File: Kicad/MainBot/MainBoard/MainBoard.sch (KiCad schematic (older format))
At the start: 35 parts, among them J1 Conn_01x02, J10 Conn_01x24, J11 01x24, J12 Conn_01x05, J13 Conn_01x03, J14 Conn_01x03, J15 Conn_01x03, J16 Conn_01x04, J17 Conn_01x04, J18 Conn_01x04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

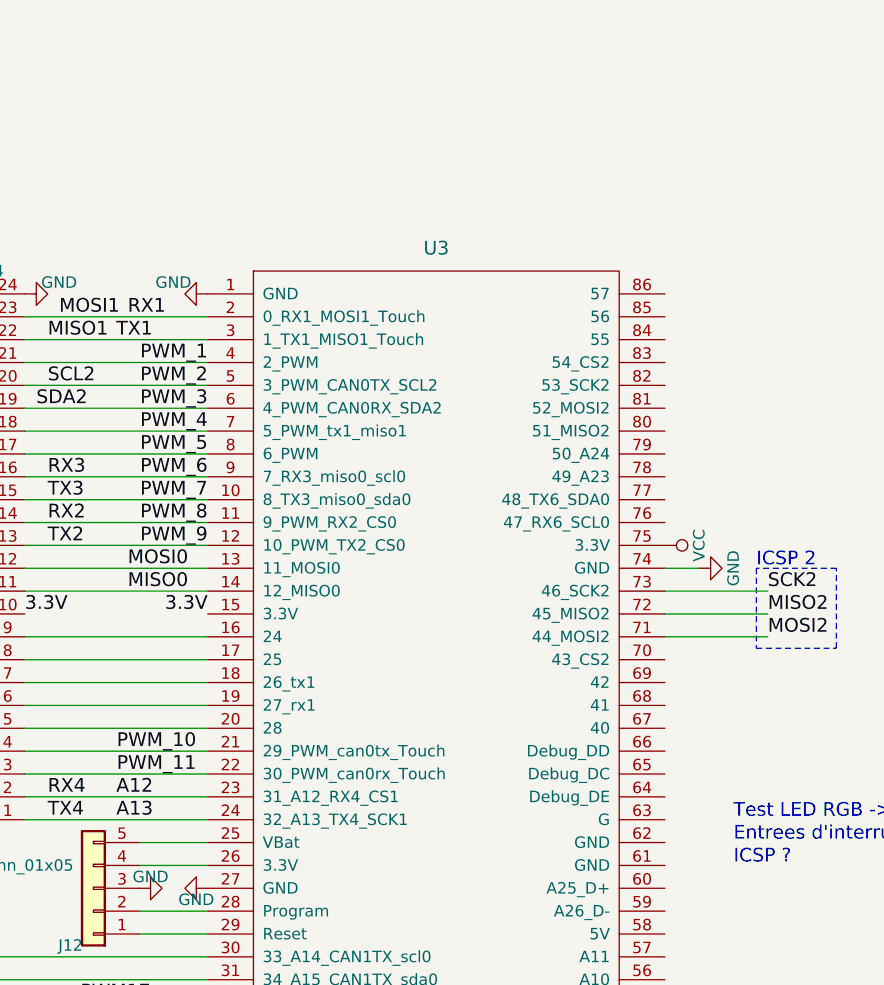
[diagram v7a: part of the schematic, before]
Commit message: Added SPI1 and SPI2 channels
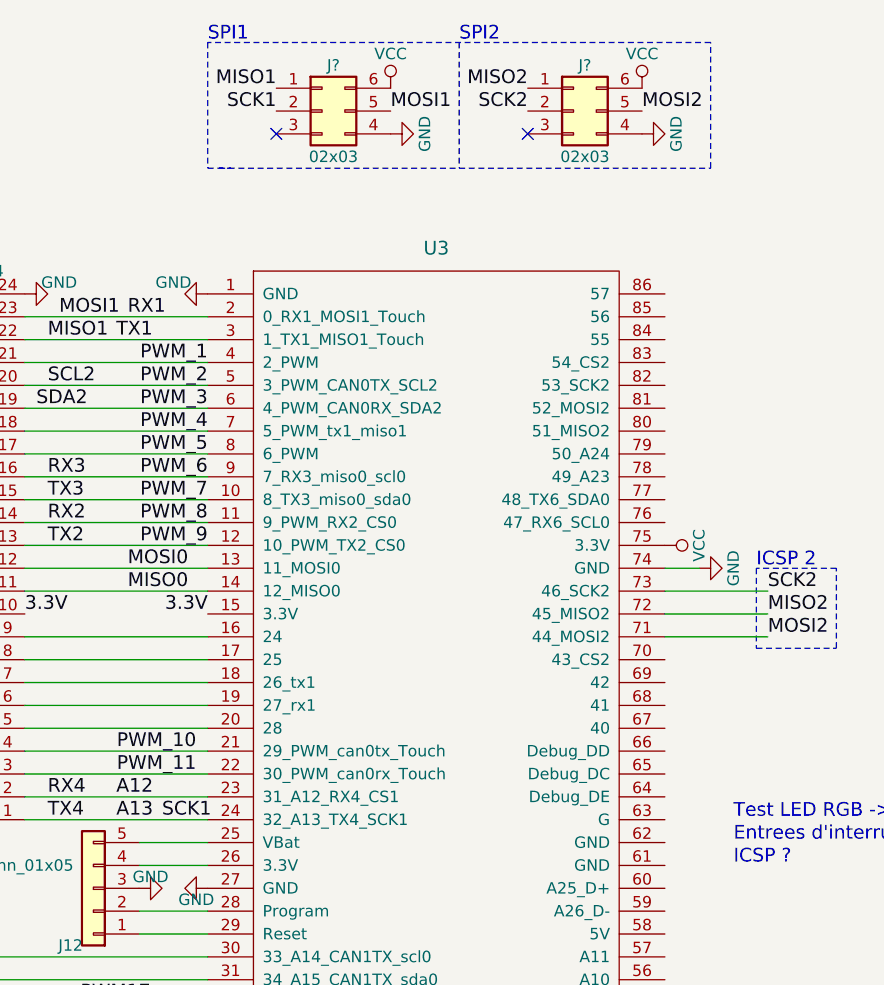
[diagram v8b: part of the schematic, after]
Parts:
- added J? (x2): 02x03, symbol Conn_02x03_Counter_Clockwise
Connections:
- net A13: now also J?.2 (Pin_2)
- net GND: now also J?.4 (Pin_4), J?.4 (Pin_4)
- net MISO1: now also J?.1 (Pin_1)
- net MISO2: now also J?.1 (Pin_1)
- net MOSI1: now also J?.5 (Pin_5)
- net MOSI2: now also J?.5 (Pin_5)
- net SCK2: now also J?.2 (Pin_2)
- net VCC: now also J?.6 (Pin_6), J?.6 (Pin_6)
- no-connect marks 20 -> 22
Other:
- note added: "SPI1\n"
- note added: "SPI2\n"
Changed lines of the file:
@@
 	1    0    0    -1
 $EndComp
+$Comp
+L Conn_02x03_Counter_Clockwise J?
+U 1 1 5C632352
+P 6300 950
+F 0 "J?" H 6350 1150 50  0000 C CNN
+F 1 "02x03" H 6350 750 50  0000 C CNN
+F 2 "" H 6300 950 50  0001 C CNN
+F 3 "" H 6300 950 50  0001 C CNN
+	1    6300 950
+	1    0    0    -1
+$EndComp
+Text Label 6100 850  2    60   ~ 0
+MISO2
+Text Label 6100 950  2    60   ~ 0
+SCK2
+Text Label 6600 950  0    60   ~ 0
+MOSI2
+$Comp
+L GND #PWR?
+U 1 1 5C632E5F
+P 6600 1050
+F 0 "#PWR?" H 6600 800 50  0001 C CNN
+F 1 "GND" H 6600 900 50  0000 C CNN
+F 2 "" H 6600 1050 50  0001 C CNN
+F 3 "" H 6600 1050 50  0001 C CNN
+	1    6600 1050
+	0    -1   -1   0
+$EndComp
+$Comp
+L VCC #PWR?
+U 1 1 5C6330FB
+P 6600 850
+F 0 "#PWR?" H 6600 700 50  0001 C CNN
+F 1 "VCC" H 6600 1000 50  0000 C CNN
+F 2 "" H 6600 850 50  0001 C CNN
+F 3 "" H 6600 850 50  0001 C CNN
+	1    6600 850
+	1    0    0    -1
+$EndComp
+Wire Notes Line
+	4750 1200 6900 1200
+Wire Notes Line
+	6900 1200 6900 650
+Wire Notes Line
+	6900 650  4700 650
+Wire Notes Line
+	5800 650  5800 1200
+Text Notes 5800 650  0    60   ~ 0
+SPI2\n
+NoConn ~ 6100 1050
+$Comp
+L Conn_02x03_Counter_Clockwise J?
+U 1 1 5C6351F9
+P 5200 950
+F 0 "J?" H 5250 1150 50  0000 C CNN
+F 1 "02x03" H 5250 750 50  0000 C CNN
+F 2 "" H 5200 950 50  0001 C CNN
+F 3 "" H 5200 950 50  0001 C CNN
+	1    5200 950
+	1    0    0    -1
+$EndComp
+$Comp
+L VCC #PWR?
+U 1 1 5C635289
+P 5500 850
+F 0 "#PWR?" H 5500 700 50  0001 C CNN
+F 1 "VCC" H 5500 1000 50  0000 C CNN
+F 2 "" H 5500 850 50  0001 C CNN
+F 3 "" H 5500 850 50  0001 C CNN
+	1    5500 850
+	1    0    0    -1
+$EndComp
+$Comp
+L GND #PWR?
+U 1 1 5C6352E7
+P 5500 1050
+F 0 "#PWR?" H 5500 800 50  0001 C CNN
+F 1 "GND" H 5500 900 50  0000 C CNN
+F 2 "" H 5500 1050 50  0001 C CNN
+F 3 "" H 5500 1050 50  0001 C CNN
+	1    5500 1050
+	0    -1   -1   0
+$EndComp
+Text Label 5000 850  2    60   ~ 0
+MISO1
+Text Label 5000 950  2    60   ~ 0
+SCK1
+Text Label 5500 950  0    60   ~ 0
+MOSI1
+NoConn ~ 5000 1050
+Wire Notes Line
+	4700 650  4700 1200
+Wire Notes Line
+	4700 1200 4800 1200
+Text Notes 4700 650  0    60   ~ 0
+SPI1\n
+Text Label 4500 4050 0    60   ~ 0
+SCK1
 $EndSCHEMATC
